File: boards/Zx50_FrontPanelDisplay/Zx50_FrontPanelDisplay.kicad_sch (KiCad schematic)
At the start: 41 parts, among them J1 Front Panel 2, J2 Front Panel, J3 Remote Off, SW1 DISP_EN, SW2 RUN, SW3 STEP, SW4 RESET, SW5 POWER, U1 HCMS-3973, U2 SN74HC595N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

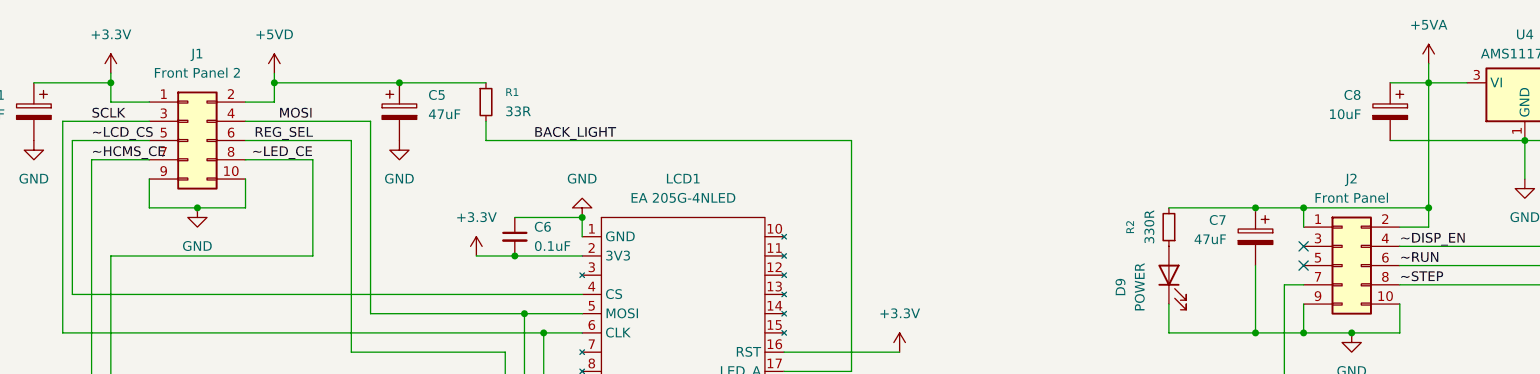
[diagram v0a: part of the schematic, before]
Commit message: Lots of updates: Work on memory card Rev C with Lattice XO3LF, finish up the front panel card firmware for the pico., add some results for the clock mezzanine Rev B.
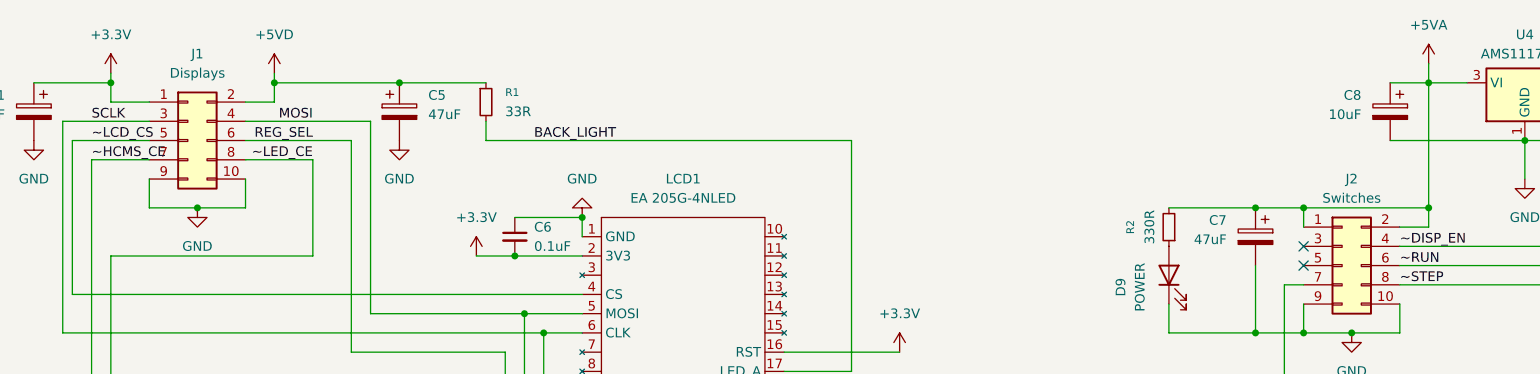
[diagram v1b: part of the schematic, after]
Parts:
- J1: value Front Panel 2 -> Displays
- J2: value Front Panel -> Switches
- RN1: Mouser_PN (none) -> 652-4116R-1LF-330
- RN2: Mouser_PN (none) -> 652-4607X-1LF-10K
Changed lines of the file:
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@@
+			)
+		)
+		(property "Mouser_PN" "652-4116R-1LF-330"
+			(at 90.17 177.8 90)
+			(effects
+				(font
+					(size 1.27 1.27)
+				)
+				(hide yes)
 			)
 		)
@@
 			)
 		)
-		(property "Value" "Front Panel 2"
+		(property "Value" "Displays"
 			(at 44.45 35.56 0)
 			(effects
@@
 			)
 		)
+		(property "Mouser_PN" "652-4607X-1LF-10K"
+			(at 233.68 52.07 0)
+			(effects
+				(font
+					(size 1.27 1.27)
+				)
+				(hide yes)
+			)
+		)
 		(pin "7"
 		)
@@
 			)
 		)
-		(property "Value" "Front Panel"
+		(property "Value" "Switches"
 			(at 196.85 52.07 0)
 			(effects

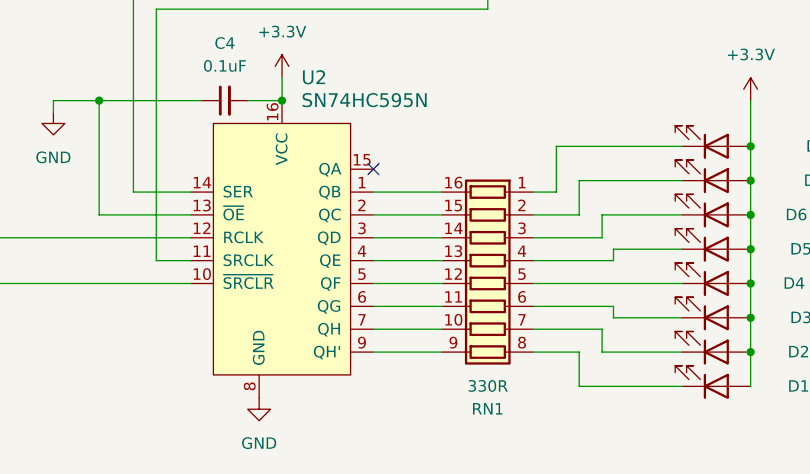
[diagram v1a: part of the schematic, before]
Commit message: board updates, front panel firmware updates, pic upates for booting
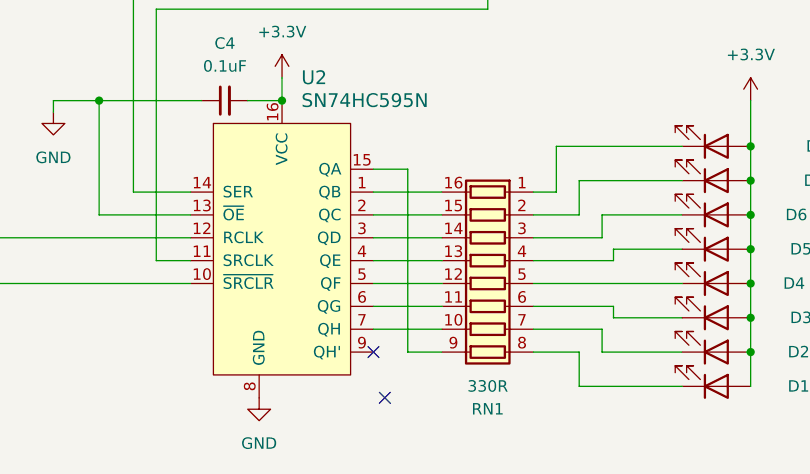
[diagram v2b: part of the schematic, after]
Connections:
- net at RN1.9 (R8.2): now also U2.15 (QA); no longer U2.9 (QH')
- no-connect marks 10 -> 11
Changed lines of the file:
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@@
+	)
+	(no_connect
+		(at 77.47 185.42)
 	)
 	(no_connect
@@
 	)
 	(no_connect
-		(at 77.47 165.1)
-	)
-	(no_connect
 		(at 267.97 91.44)
 	)
@@
 	)
 	(no_connect
+		(at 78.74 190.5)
+	)
+	(no_connect
 		(at 231.14 57.15)
 	)
@@
 	(wire
 		(pts
+			(xy 81.28 185.42) (xy 81.28 165.1)
+		)
+		(stroke
+			(width 0)
+			(type default)
+		)
+	)
+	(wire
+		(pts
 			(xy 119.38 177.8) (xy 119.38 181.61)
 		)
@@
 	(wire
 		(pts
+			(xy 77.47 165.1) (xy 81.28 165.1)
+		)
+		(stroke
+			(width 0)
+			(type default)
+		)
+	)
+	(wire
+		(pts
 			(xy 53.34 147.32) (xy 53.34 175.26)
 		)
@@
 	(wire
 		(pts
+			(xy 85.09 185.42) (xy 81.28 185.42)
+		)
+		(stroke
+			(width 0)
+			(type default)
+		)
+	)
+	(wire
+		(pts
 			(xy 46.99 157.48) (xy 58.42 157.48)
 		)
@@
 		)
 		(stroke
-			(width 0)
-			(type default)
-		)
-	)
-	(wire
-		(pts
-			(xy 77.47 185.42) (xy 85.09 185.42)
-		)
-		(stroke
